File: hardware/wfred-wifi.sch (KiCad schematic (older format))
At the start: 11 parts, among them K201 UART_ESP, P201 ESP_BOOTLOAD, U201 ESP-12E

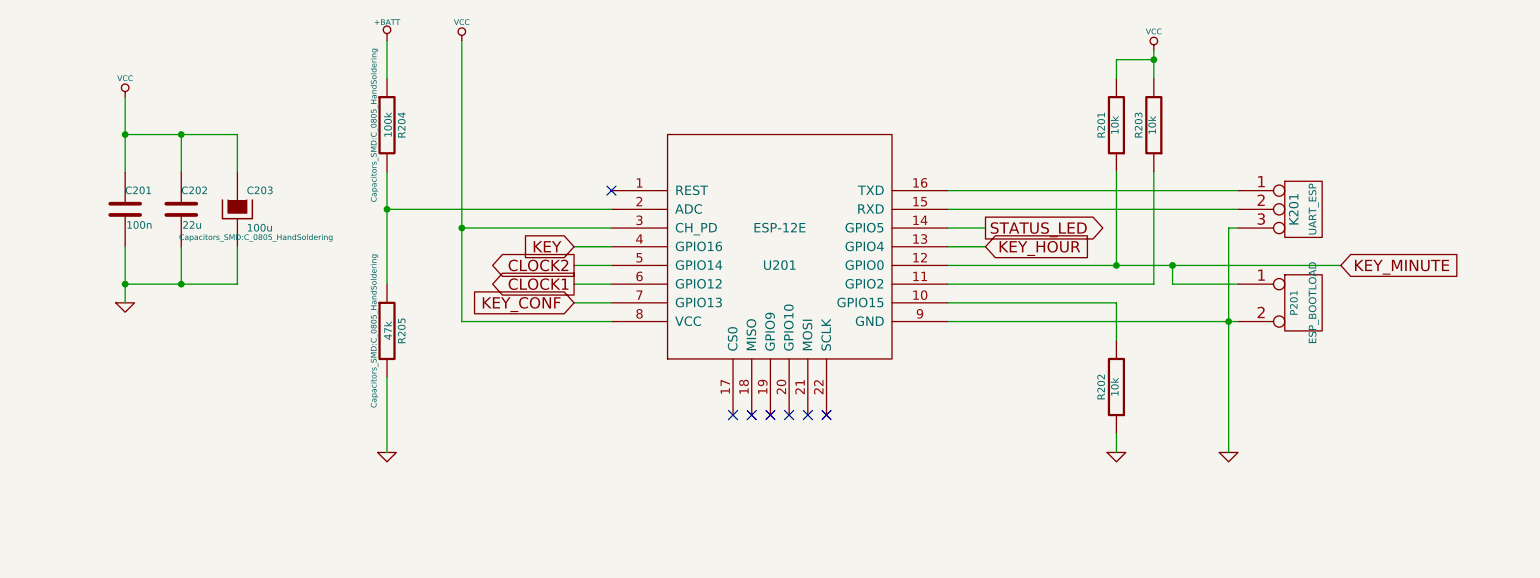
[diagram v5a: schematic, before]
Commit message: Add second clock output...
...while removing (so far) unused key
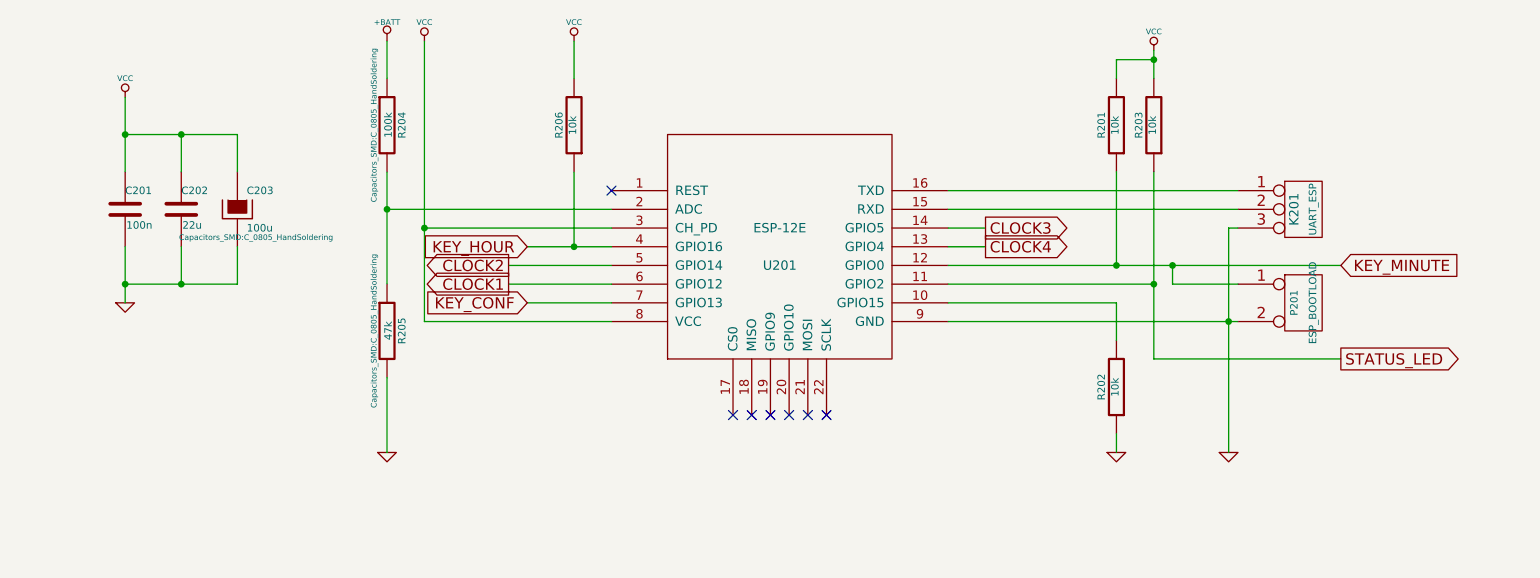
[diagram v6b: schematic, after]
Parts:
- added R206: 10k, Capacitors_SMD:C_0805_HandSoldering, symbol R
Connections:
- net KEY is gone; now on net KEY_HOUR: U201.4 (GPIO16)
- net KEY_HOUR: now also R206.1; no longer U201.13 (GPIO4)
- net STATUS_LED: now also R203.1, U201.11 (GPIO2); no longer U201.14 (GPIO5)
- net VCC: now also R206.2
- new net CLOCK3: U201.14 (GPIO5)
- new net CLOCK4: U201.13 (GPIO4)
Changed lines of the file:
@@
 EESchema Schematic File Version 2
+LIBS:wfred_loconet_clock-rescue
 LIBS:power
 LIBS:device
@@
 L VCC #PWR011
 U 1 1 5A11E004
-P 3000 1500
-F 0 "#PWR011" H 3000 1600 30  0001 C CNN
-F 1 "VCC" H 3000 1600 30  0000 C CNN
-F 2 "" H 3000 1500 60  0001 C CNN
-F 3 "" H 3000 1500 60  0001 C CNN
-	1    3000 1500
-	1    0    0    -1
-$EndComp
-Wire Wire Line
-	3000 1500 3000 3000
-Wire Wire Line
-	3000 3000 3800 3000
-Wire Wire Line
-	3800 2500 3000 2500
-Connection ~ 3000 2500
+P 2800 1500
+F 0 "#PWR011" H 2800 1600 30  0001 C CNN
+F 1 "VCC" H 2800 1600 30  0000 C CNN
+F 2 "" H 2800 1500 60  0001 C CNN
+F 3 "" H 2800 1500 60  0001 C CNN
+	1    2800 1500
+	1    0    0    -1
+$EndComp
+Wire Wire Line
+	2800 1500 2800 3000
+Wire Wire Line
+	2800 3000 3800 3000
+Wire Wire Line
+	3800 2500 2800 2500
+Connection ~ 2800 2500
 $Comp
 L GND #PWR012
@@
 	6700 2800 5600 2800
 Wire Wire Line
-	5600 2900 6500 2900
-Wire Wire Line
 	6500 2700 6500 2200
 Connection ~ 6500 2700
 Wire Wire Line
-	6700 2200 6700 2800
+	6700 2200 6700 3200
 Wire Wire Line
 	6500 1700 6500 1600
@@
 Connection ~ 1200 2800
 NoConn ~ 3800 2300
-Text GLabel 5800 2500 2    60   Output ~ 0
+Text GLabel 7700 3200 2    60   Output ~ 0
 STATUS_LED
 Wire Wire Line
-	3600 2700 3800 2700
-Text GLabel 3600 2700 0    60   Output ~ 0
+	3250 2700 3800 2700
+Text GLabel 3250 2700 0    60   Output ~ 0
 CLOCK2
-Text GLabel 3600 2900 0    60   Input ~ 0
+Text GLabel 3350 2900 0    60   Input ~ 0
 KEY_CONF
 $Comp
@@
 Wire Wire Line
 	2600 2400 3800 2400
-Text GLabel 3600 2800 0    60   Output ~ 0
+Text GLabel 3250 2800 0    60   Output ~ 0
 CLOCK1
 Wire Wire Line
-	3600 2900 3800 2900
+	3350 2900 3800 2900
 Wire Wire Line
 	5600 2500 5800 2500
@@
 	2600 3300 2600 3700
 Wire Wire Line
-	3800 2800 3600 2800
-Text GLabel 3600 2600 0    60   Input ~ 0
-KEY
-Wire Wire Line
-	3600 2600 3800 2600
-Text GLabel 5800 2600 2    60   Input ~ 0
+	3800 2800 3250 2800
+Text GLabel 3350 2600 0    60   Input ~ 0
 KEY_HOUR
+Wire Wire Line
+	3350 2600 3800 2600
 Text GLabel 7700 2700 2    60   Input ~ 0
 KEY_MINUTE
@@
 Wire Wire Line
 	5800 2600 5600 2600
+Wire Wire Line
+	6700 3200 7700 3200
+Connection ~ 6700 2800
+Text GLabel 5800 2500 2    60   Output ~ 0
+CLOCK3
+Text GLabel 5800 2600 2    60   Output ~ 0
+CLOCK4
+Wire Wire Line
+	6500 2900 5600 2900
+$Comp
+L R R206
+U 1 1 5D44B97B
+P 3600 1950
+F 0 "R206" V 3680 1950 40  0000 C CNN
+F 1 "10k" V 3607 1951 40  0000 C CNN
+F 2 "Capacitors_SMD:C_0805_HandSoldering" V 3530 1950 30  0001 C CNN
+F 3 "" H 3600 1950 30  0000 C CNN
+F 4 "603-RC0805JR-0710KL" V 3600 1950 60  0001 C CNN "Mouser"
+	1    3600 1950
+	-1   0    0    1
+$EndComp
+$Comp
+L VCC #PWR019
+U 1 1 5D44BB12
+P 3600 1500
+F 0 "#PWR019" H 3600 1600 30  0001 C CNN
+F 1 "VCC" H 3600 1600 30  0000 C CNN
+F 2 "" H 3600 1500 60  0001 C CNN
+F 3 "" H 3600 1500 60  0001 C CNN
+	1    3600 1500
+	1    0    0    -1
+$EndComp
+Wire Wire Line
+	3600 1500 3600 1700
+Wire Wire Line
+	3600 2200 3600 2600
+Connection ~ 3600 2600
 $EndSCHEMATC

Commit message: Opened schematic and pcb with kicad 5.1.5...
...to update library table
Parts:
- C201, C202: symbol C -> wfred_loconet_clock-rescue:C
- C203: symbol CAPAPOL -> wfred_loconet_clock-rescue:CAPAPOL
- K201: symbol CONN_3 -> wfred_loconet_clock-rescue:CONN_3
- P201: symbol CONN_2 -> wfred_loconet_clock-rescue:CONN_2
- R201, R202, R203, R204, R205, R206: symbol R -> wfred_loconet_clock-rescue:R
- U201: symbol ESP-12E -> wfred_loconet_clock-rescue:ESP-12E
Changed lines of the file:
@@
-EESchema Schematic File Version 2
-LIBS:wfred_loconet_clock-rescue
-LIBS:power
-LIBS:device
-LIBS:transistors
-LIBS:conn
-LIBS:linear
-LIBS:regul
-LIBS:74xx
-LIBS:cmos4000
-LIBS:adc-dac
-LIBS:memory
-LIBS:xilinx
-LIBS:microcontrollers
-LIBS:dsp
-LIBS:microchip
-LIBS:analog_switches
-LIBS:motorola
-LIBS:texas
-LIBS:intel
-LIBS:audio
-LIBS:interface
-LIBS:digital-audio
-LIBS:philips
-LIBS:display
-LIBS:cypress
-LIBS:siliconi
-LIBS:opto
-LIBS:atmel
-LIBS:contrib
-LIBS:valves
-LIBS:my_devices
-LIBS:ESP8266
-LIBS:wfred_loconet_clock-cache
-EELAYER 25 0
+EESchema Schematic File Version 4
+EELAYER 30 0
 EELAYER END
 $Descr A4 11693 8268
@@
 $EndDescr
 $Comp
-L ESP-12E U201
+L wfred_loconet_clock-rescue:ESP-12E U201
 U 1 1 5A11AA62
 P 4700 2600
@@
 NoConn ~ 4950 3500
 $Comp
-L VCC #PWR011
+L wfred_loconet_clock-rescue:VCC #PWR011
 U 1 1 5A11E004
 P 2800 1500
@@
 $EndComp
 Wire Wire Line
-	2800 1500 2800 3000
+	2800 1500 2800 2500
 Wire Wire Line
 	2800 3000 3800 3000
@@
 Connection ~ 2800 2500
 $Comp
-L GND #PWR012
+L wfred_loconet_clock-rescue:GND #PWR012
 U 1 1 5A11E30D
 P 7100 3700
@@
 $EndComp
 Wire Wire Line
-	7100 2500 7100 3700
-Wire Wire Line
-	5600 3000 7150 3000
+	7100 2500 7100 3000
+Wire Wire Line
+	5600 3000 7100 3000
 Connection ~ 7100 3000
 $Comp
-L VCC #PWR013
+L wfred_loconet_clock-rescue:VCC #PWR013
 U 1 1 5A11E4AA
 P 6700 1550
@@
 	5600 2400 7150 2400
 $Comp
-L CONN_3 K201
+L wfred_loconet_clock-rescue:CONN_3 K201
 U 1 1 5A11EE74
 P 7500 2400
@@
 	7150 2500 7100 2500
 $Comp
-L CONN_2 P201
+L wfred_loconet_clock-rescue:CONN_2 P201
 U 1 1 5A11F720
 P 7500 2900
@@
 $EndComp
 Wire Wire Line
-	5600 2700 7700 2700
-$Comp
-L R R201
+	5600 2700 6500 2700
+$Comp
+L wfred_loconet_clock-rescue:R R201
 U 1 1 5A11FF91
 P 6500 1950
@@
 $EndComp
 $Comp
-L R R202
+L wfred_loconet_clock-rescue:R R202
 U 1 1 5A11FFE4
 P 6500 3350
@@
 $EndComp
 $Comp
-L R R203
+L wfred_loconet_clock-rescue:R R203
 U 1 1 5A120047
 P 6700 1950
@@
 Connection ~ 6500 2700
 Wire Wire Line
-	6700 2200 6700 3200
+	6700 2200 6700 2800
 Wire Wire Line
 	6500 1700 6500 1600
 Wire Wire Line
-	6700 1550 6700 1700
+	6700 1550 6700 1600
 Connection ~ 6700 1600
 Wire Wire Line
 	6500 2900 6500 3100
 $Comp
-L GND #PWR014
+L wfred_loconet_clock-rescue:GND #PWR014
 U 1 1 5A120E87
 P 6500 3700
@@
 	6500 1600 6700 1600
 $Comp
-L C C201
+L wfred_loconet_clock-rescue:C C201
 U 1 1 5A127BCA
 P 1200 2400
@@
 $EndComp
 $Comp
-L VCC #PWR015
+L wfred_loconet_clock-rescue:VCC #PWR015
 U 1 1 5A127C0E
 P 1200 1800
@@
 $EndComp
 Wire Wire Line
-	1200 1800 1200 2200
-$Comp
-L GND #PWR016
+	1200 1800 1200 2000
+$Comp
+L wfred_loconet_clock-rescue:GND #PWR016
 U 1 1 5A127CDB
 P 1200 2900
@@
 $EndComp
 Wire Wire Line
-	1200 2600 1200 2900
-$Comp
-L C C202
+	1200 2600 1200 2800
+$Comp
+L wfred_loconet_clock-rescue:C C202
 U 1 1 5A199174
 P 1500 2400
@@
 $EndComp
 Wire Wire Line
-	1200 2000 1800 2000
+	1200 2000 1500 2000
 Wire Wire Line
 	1500 2000 1500 2200
@@
 	1500 2600 1500 2800
 Wire Wire Line
-	1200 2800 1800 2800
+	1200 2800 1500 2800
 Connection ~ 1200 2800
 NoConn ~ 3800 2300
@@
 KEY_CONF
 $Comp
-L CAPAPOL C203
+L wfred_loconet_clock-rescue:CAPAPOL C203
 U 1 1 5C82A7FA
 P 1800 2400
@@
 Connection ~ 1500 2800
 $Comp
-L +BATT #PWR017
+L wfred_loconet_clock-rescue:+BATT #PWR017
 U 1 1 5C82B48A
 P 2600 1500
+AR Path="/5C82B48A" Ref="#PWR017"  Part="1"
+AR Path="/5A122619/5C82B48A" Ref="#PWR017"  Part="1"
 F 0 "#PWR017" H 2600 1450 20  0001 C CNN
 F 1 "+BATT" H 2600 1600 30  0000 C CNN
@@
 	5600 2500 5800 2500
 $Comp
-L GND #PWR018
+L wfred_loconet_clock-rescue:GND #PWR018
 U 1 1 5C85530A
 P 2600 3700
@@
 $EndComp
 $Comp
-L R R204
+L wfred_loconet_clock-rescue:R R204
 U 1 1 5C85534D
 P 2600 1950
@@
 $EndComp
 $Comp
-L R R205
+L wfred_loconet_clock-rescue:R R205
 U 1 1 5C855376
 P 2600 3050
@@
 	2600 1500 2600 1700
 Wire Wire Line
-	2600 2200 2600 2800
+	2600 2200 2600 2400
 Connection ~ 2600 2400
 Wire Wire Line
@@
 KEY_HOUR
 Wire Wire Line
-	3350 2600 3800 2600
+	3350 2600 3600 2600
 Text GLabel 7700 2700 2    60   Input ~ 0
 KEY_MINUTE
@@
 	6500 2900 5600 2900
 $Comp
-L R R206
+L wfred_loconet_clock-rescue:R R206
 U 1 1 5D44B97B
 P 3600 1950
@@
 $EndComp
 $Comp
-L VCC #PWR019
+L wfred_loconet_clock-rescue:VCC #PWR019
 U 1 1 5D44BB12
 P 3600 1500
@@
 	3600 2200 3600 2600
 Connection ~ 3600 2600
+Wire Wire Line
+	2800 2500 2800 3000
+Wire Wire Line
+	7100 3000 7100 3700
+Wire Wire Line
+	7100 3000 7150 3000
+Wire Wire Line
+	6500 2700 6800 2700
+Wire Wire Line
+	6700 1600 6700 1700
+Wire Wire Line
+	1200 2000 1200 2200
+Wire Wire Line
+	1200 2800 1200 2900
+Wire Wire Line
+	1500 2000 1800 2000
+Wire Wire Line
+	1500 2800 1800 2800
+Wire Wire Line
+	2600 2400 2600 2800
+Wire Wire Line
+	6800 2700 7700 2700
+Wire Wire Line
+	6700 2800 6700 3200
+Wire Wire Line
+	3600 2600 3800 2600
 $EndSCHEMATC
